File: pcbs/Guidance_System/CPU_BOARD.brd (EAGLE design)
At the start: 100 x 52.1 mm, 29 parts, among them J1 22-27-2081-08, J10 22-27-2081-08, J11 22-27-2081-08, J12 22-27-2081-08, J13 22-27-2081-08, J14 22-27-2081-08, J15 22-27-2041-04, J16 22-27-2041-04, J17 22-27-2021-02, J2 22-27-2021-02, J3 22-27-2041-04, J4 22-27-2041-04, J5 22-27-2081-08, J6 22-27-2021-02, J7 22-27-2081-08, J8 22-27-2021-02, J9 22-27-2021-02

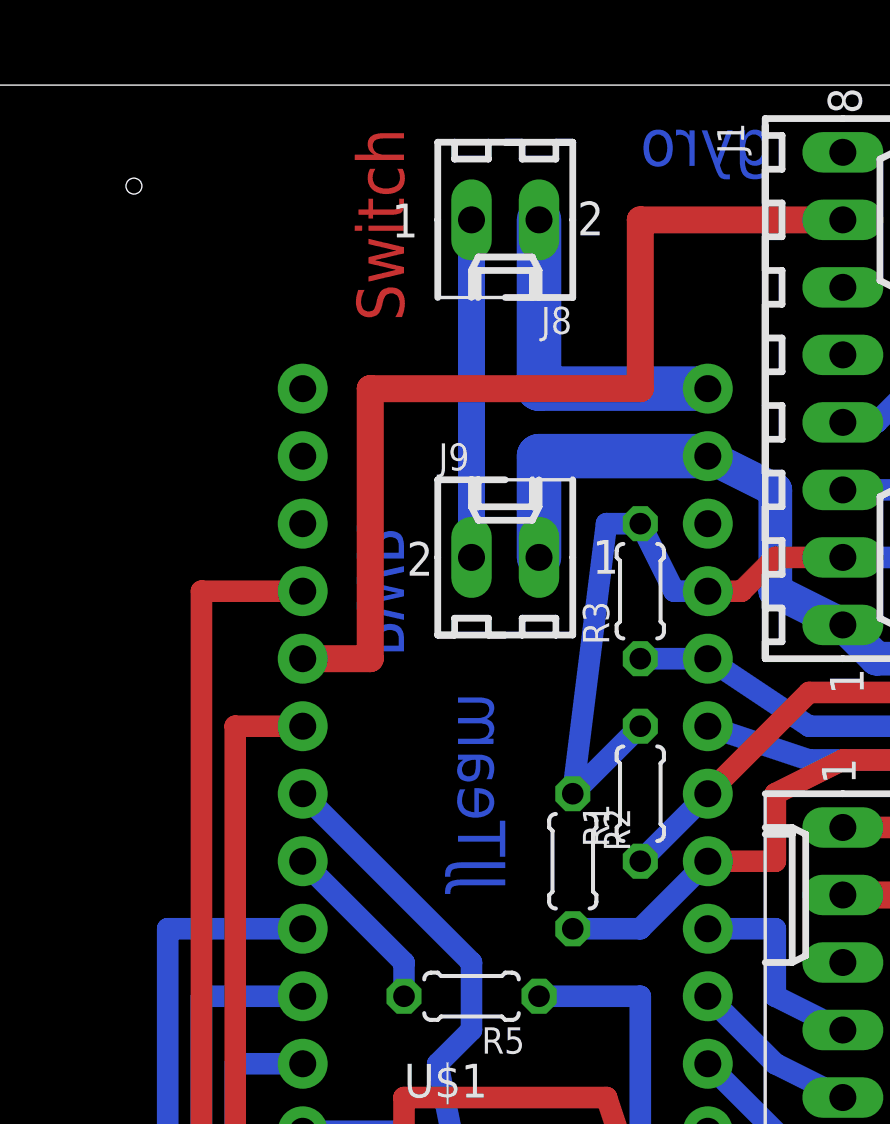
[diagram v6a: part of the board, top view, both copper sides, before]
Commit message: * Moved power socket to between Gyro and FRAM
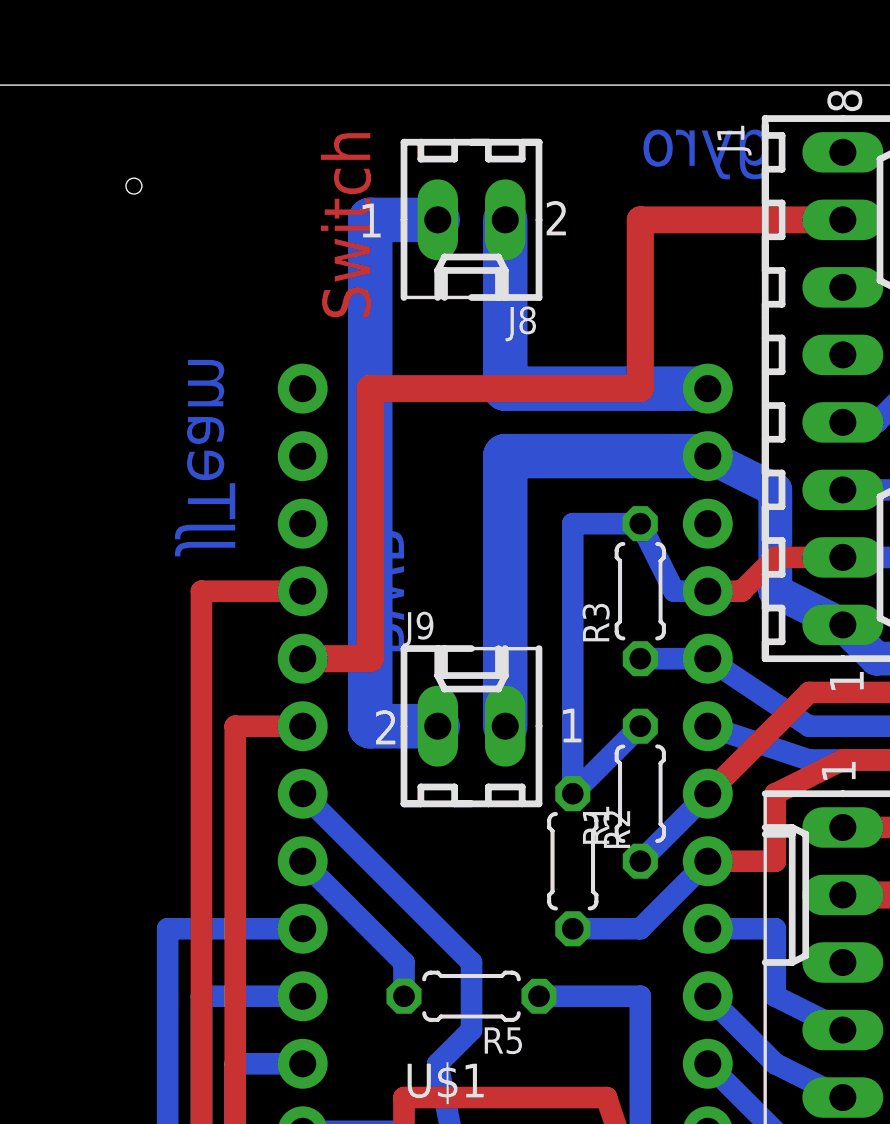
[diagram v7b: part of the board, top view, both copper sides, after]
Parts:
- moved J9 6.48 mm to (69.8, 53.3)
- moved J8 1.27 mm to (69.8, 72.4)
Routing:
- net VCC: track 12.7 -> 24.1 mm
- net N$24: track 43.6 -> 51.2 mm
- net N$5: track 12.7 -> 14.0 mm
- net N$3: track 119.1 -> 120.3 mm

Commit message: * Minor adjustments
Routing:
- net N$32: track 90.7 -> 88.7 mm
- net N$35: track 75.0 -> 76.8 mm
- net N$44: track 30.0 -> 29.2 mm
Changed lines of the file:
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@@
 <wire x1="0" y1="77.46" x2="0" y2="25.4" width="0" layer="20"/>
 <text x="19.05" y="44.45" size="1.778" layer="1">S1 Driver</text>
-<text x="27.94" y="66.04" size="1.778" layer="1" rot="R180">S2 Driver</text>
+<text x="27.94" y="67.31" size="1.778" layer="1" rot="R180">S2 Driver</text>
 <hole x="3.81" y="30.48" drill="0.6"/>
 <hole x="57.15" y="30.48" drill="0.6"/>
@@
 <text x="99.06" y="59.69" size="1.778" layer="1" rot="R90">S1 Sense</text>
 <text x="99.06" y="48.26" size="1.778" layer="1" rot="R90">S2 Sense</text>
-<text x="67.31" y="60.96" size="1.778" layer="16" rot="MR270">PWR</text>
+<text x="68.58" y="57.15" size="1.27" layer="16" rot="MR90">PWR</text>
 <text x="66.04" y="68.58" size="1.778" layer="1" rot="R90">Switch</text>
-<text x="88.9" y="74.93" size="1.778" layer="1">i2c</text>
+<text x="95.25" y="71.12" size="1.778" layer="1" rot="R90">i2c</text>
 <text x="99.06" y="35.56" size="1.778" layer="1" rot="R90">Status</text>
 <text x="35.56" y="69.85" size="1.778" layer="16" rot="MR270">JJTeam</text>
 <text x="60.96" y="67.31" size="1.778" layer="16" rot="MR270">JJTeam</text>
 <text x="33.02" y="43.18" size="1.778" layer="16" rot="MR0">S1</text>
-<text x="33.02" y="63.5" size="1.778" layer="16" rot="MR0">S2</text>
+<text x="31.75" y="63.5" size="1.778" layer="16" rot="MR0">S2</text>
 <text x="76.2" y="76.2" size="1.778" layer="16" rot="MR180">gyro</text>
 <text x="87.63" y="41.91" size="1.778" layer="16" rot="MR90">fram</text>
@@
 <contactref element="J10" pad="3"/>
 <contactref element="J13" pad="3"/>
-<wire x1="29.21" y1="72.39" x2="29.21" y2="64.77" width="1.6764" layer="16"/>
-<wire x1="29.21" y1="64.77" x2="19.05" y2="64.77" width="0.8128" layer="16"/>
+<wire x1="29.21" y1="72.39" x2="29.21" y2="68.58" width="0.8128" layer="16"/>
+<wire x1="29.21" y1="68.58" x2="26.67" y2="64.77" width="0.8128" layer="16"/>
+<wire x1="26.67" y1="64.77" x2="19.05" y2="64.77" width="0.8128" layer="16"/>
 <wire x1="19.05" y1="64.77" x2="19.05" y2="59.69" width="0.8128" layer="16"/>
 <wire x1="19.05" y1="59.69" x2="19.05" y2="57.15" width="1.6764" layer="16"/>
@@
 <wire x1="19.05" y1="39.37" x2="19.05" y2="40.64" width="0.4064" layer="16"/>
 <wire x1="19.05" y1="40.64" x2="19.05" y2="44.45" width="0.8128" layer="16"/>
-<wire x1="19.05" y1="44.45" x2="29.21" y2="44.45" width="0.8128" layer="16"/>
-<wire x1="29.21" y1="44.45" x2="29.21" y2="45.72" width="0.8128" layer="16"/>
-<wire x1="29.21" y1="45.72" x2="29.21" y2="52.07" width="1.6764" layer="16"/>
+<wire x1="19.05" y1="44.45" x2="26.67" y2="44.45" width="0.8128" layer="16"/>
+<wire x1="26.67" y1="44.45" x2="29.21" y2="46.99" width="0.8128" layer="16"/>
+<wire x1="29.21" y1="46.99" x2="29.21" y2="52.07" width="0.8128" layer="16"/>
 <wire x1="25.4" y1="31.75" x2="34.29" y2="31.75" width="0.8128" layer="16"/>
-<wire x1="34.29" y1="31.75" x2="34.29" y2="45.72" width="0.8128" layer="16"/>
-<wire x1="34.29" y1="45.72" x2="29.21" y2="45.72" width="0.8128" layer="16"/>
+<wire x1="34.29" y1="31.75" x2="34.29" y2="46.99" width="0.8128" layer="16"/>
+<wire x1="34.29" y1="46.99" x2="29.21" y2="46.99" width="0.8128" layer="16"/>
 </signal>
 <signal name="N$33">
@@
 <wire x1="11.43" y1="59.69" x2="13.97" y2="63.5" width="0.8128" layer="16"/>
 <wire x1="13.97" y1="63.5" x2="13.97" y2="66.04" width="0.8128" layer="16"/>
-<wire x1="13.97" y1="66.04" x2="26.67" y2="66.04" width="0.8128" layer="16"/>
-<wire x1="26.67" y1="66.04" x2="26.67" y2="72.39" width="0.8128" layer="16"/>
+<wire x1="13.97" y1="66.04" x2="25.4" y2="66.04" width="0.8128" layer="16"/>
+<wire x1="25.4" y1="66.04" x2="26.67" y2="67.31" width="0.8128" layer="16"/>
+<wire x1="26.67" y1="67.31" x2="26.67" y2="72.39" width="0.8128" layer="16"/>
 </signal>
 <signal name="N$31">
@@
 <wire x1="13.97" y1="54.61" x2="12.7" y2="54.61" width="0.8128" layer="1"/>
 <wire x1="12.7" y1="54.61" x2="11.43" y2="52.07" width="0.8128" layer="1"/>
-<wire x1="13.97" y1="46.99" x2="11.43" y2="49.53" width="0.8128" layer="1"/>
+<wire x1="13.97" y1="48.26" x2="11.43" y2="49.53" width="0.8128" layer="1"/>
 <wire x1="11.43" y1="49.53" x2="11.43" y2="52.07" width="0.8128" layer="1"/>
-<wire x1="13.97" y1="39.37" x2="13.97" y2="46.99" width="0.8128" layer="1"/>
-<wire x1="13.97" y1="46.99" x2="34.29" y2="46.99" width="0.8128" layer="1"/>
-<wire x1="34.29" y1="46.99" x2="34.29" y2="34.29" width="0.8128" layer="1"/>
+<wire x1="13.97" y1="39.37" x2="13.97" y2="48.26" width="0.8128" layer="1"/>
+<wire x1="13.97" y1="48.26" x2="34.29" y2="48.26" width="0.8128" layer="1"/>
+<wire x1="34.29" y1="48.26" x2="34.29" y2="34.29" width="0.8128" layer="1"/>
 <wire x1="34.29" y1="34.29" x2="17.78" y2="34.29" width="0.8128" layer="1"/>
 <wire x1="17.78" y1="34.29" x2="17.78" y2="31.75" width="0.8128" layer="1"/>
@@
 </signal>
 </signals>
+<errors>
+</errors>
 </board>
 </drawing>
